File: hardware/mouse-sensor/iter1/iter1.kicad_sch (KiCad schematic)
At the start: 13 parts

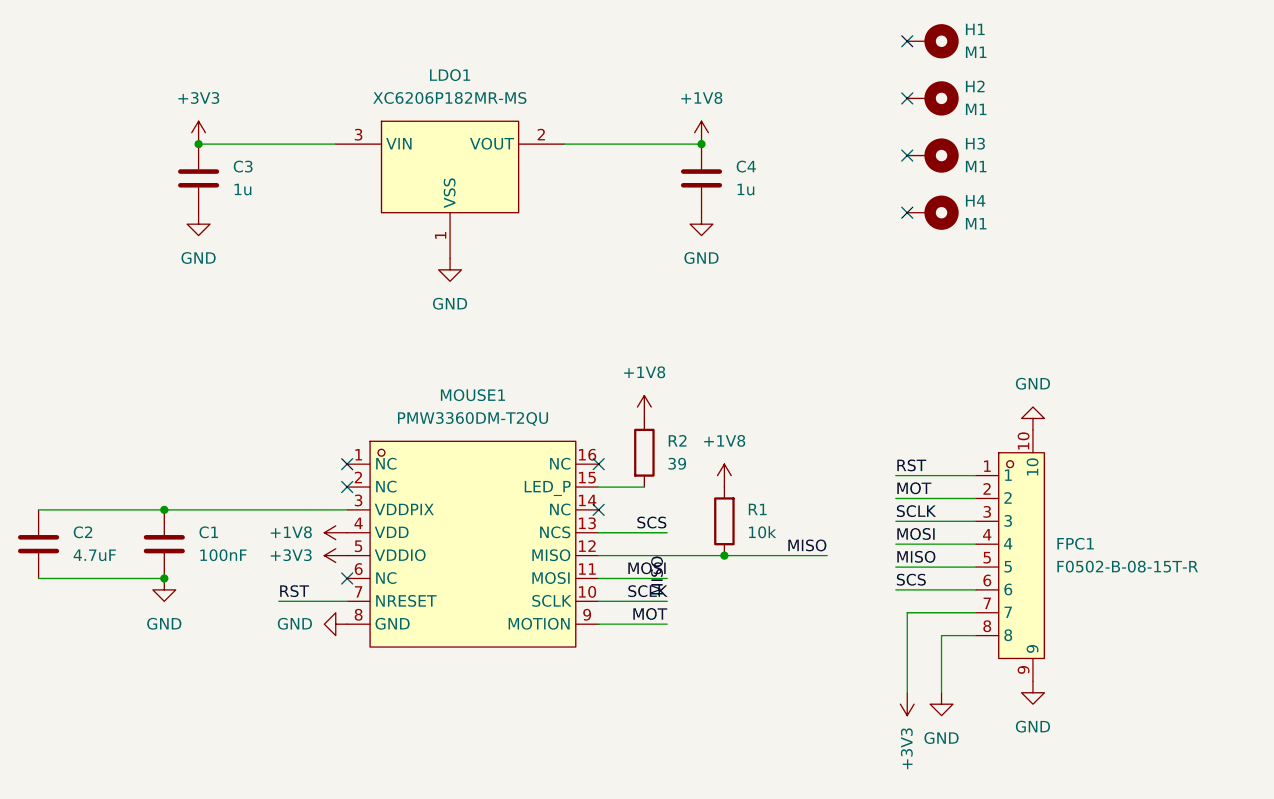
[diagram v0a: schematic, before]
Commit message: symmetric handsolderable less compact mouse sensor breakout
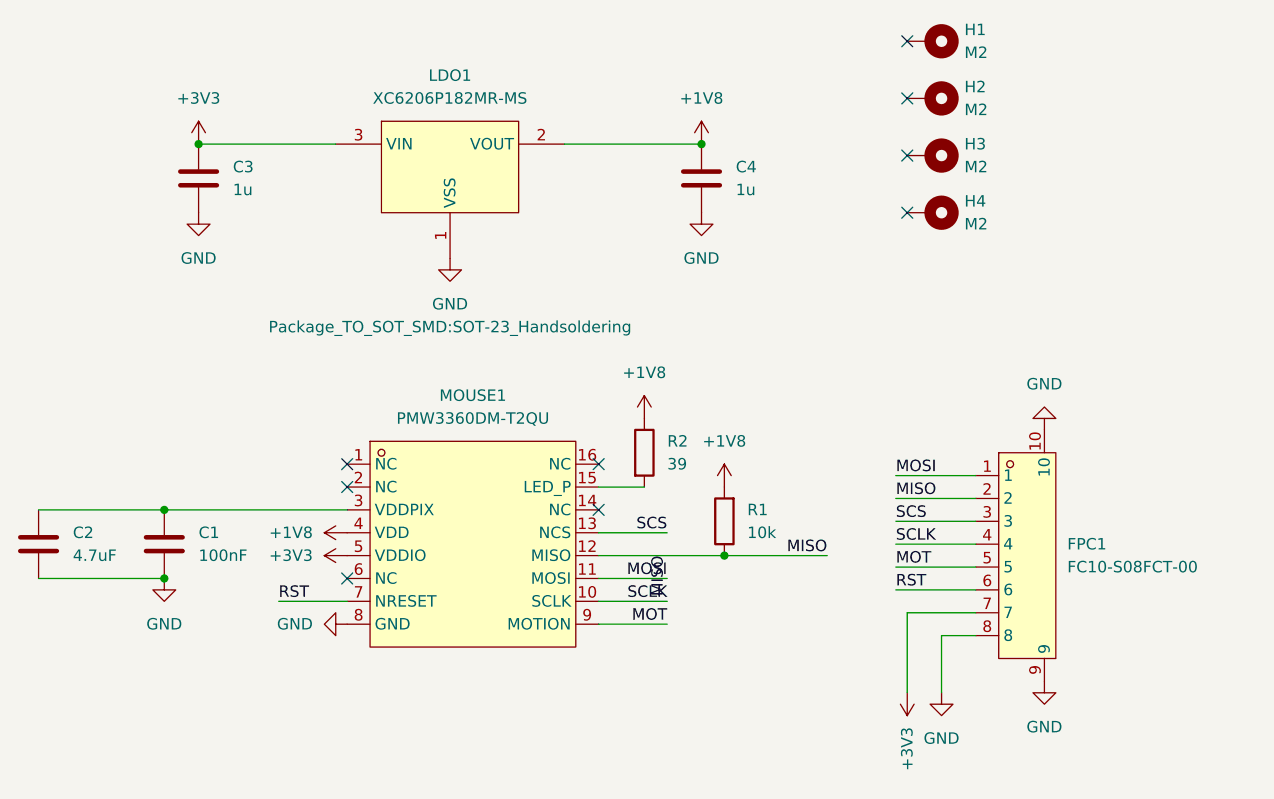
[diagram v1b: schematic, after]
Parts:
- removed FPC1: F0502-B-08-15T-R, EasyEDA:FPC-SMD_8P-P0.50_F0502-B-08-15T-R, symbol EasyEDA:F0502-B-08-15T-R
- added FPC1: FC10-S08FCT-00, EasyEDA:FPC-SMD_8P-P1.00_DEALON_FC10-S08FCT-00, symbol EasyEDA:FC10-S08FCT-00
- C1, C2, C3, C4: footprint Capacitor_SMD:C_0603_1608Metric -> Capacitor_SMD:C_0805_2012Metric_Pad1.18x1.45mm_HandSolder
- H1, H2, H3, H4: value M1 -> M2; footprint CustomMountingHole:MountingHole_1.2mm_M1_Pad -> MountingHole:MountingHole_2.2mm_M2_Pad_Via
- LDO1: footprint Package_TO_SOT_SMD:SOT-23-3 -> Package_TO_SOT_SMD:SOT-23_Handsoldering
- R1, R2: footprint PCM_Resistor_SMD_AKL:R_0603_1608Metric -> PCM_Resistor_SMD_AKL:R_0805_2012Metric_Pad1.15x1.40mm_HandSolder
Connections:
- net +3V3: now also FPC1.7
- net GND: now also FPC1.10, FPC1.8, FPC1.9
- net MISO: now also FPC1.2
- net MOSI: now also FPC1.1
- net MOT: now also FPC1.5
- net RST: now also FPC1.6
- net SCLK: now also FPC1.4
- net SCS: now also FPC1.3
